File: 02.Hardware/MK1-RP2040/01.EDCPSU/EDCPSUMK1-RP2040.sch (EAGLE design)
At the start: 182 parts, among them J6 Display, Q2 2N7002PW, Q4 2N7002PW, Q9 2N7002PW, U1 RP2040TR7, U11 AP63203, U12 AP64501SP-13, U2 MCP4725, U3 SN74AC14PWR, U4 MAX9938FEUK+T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

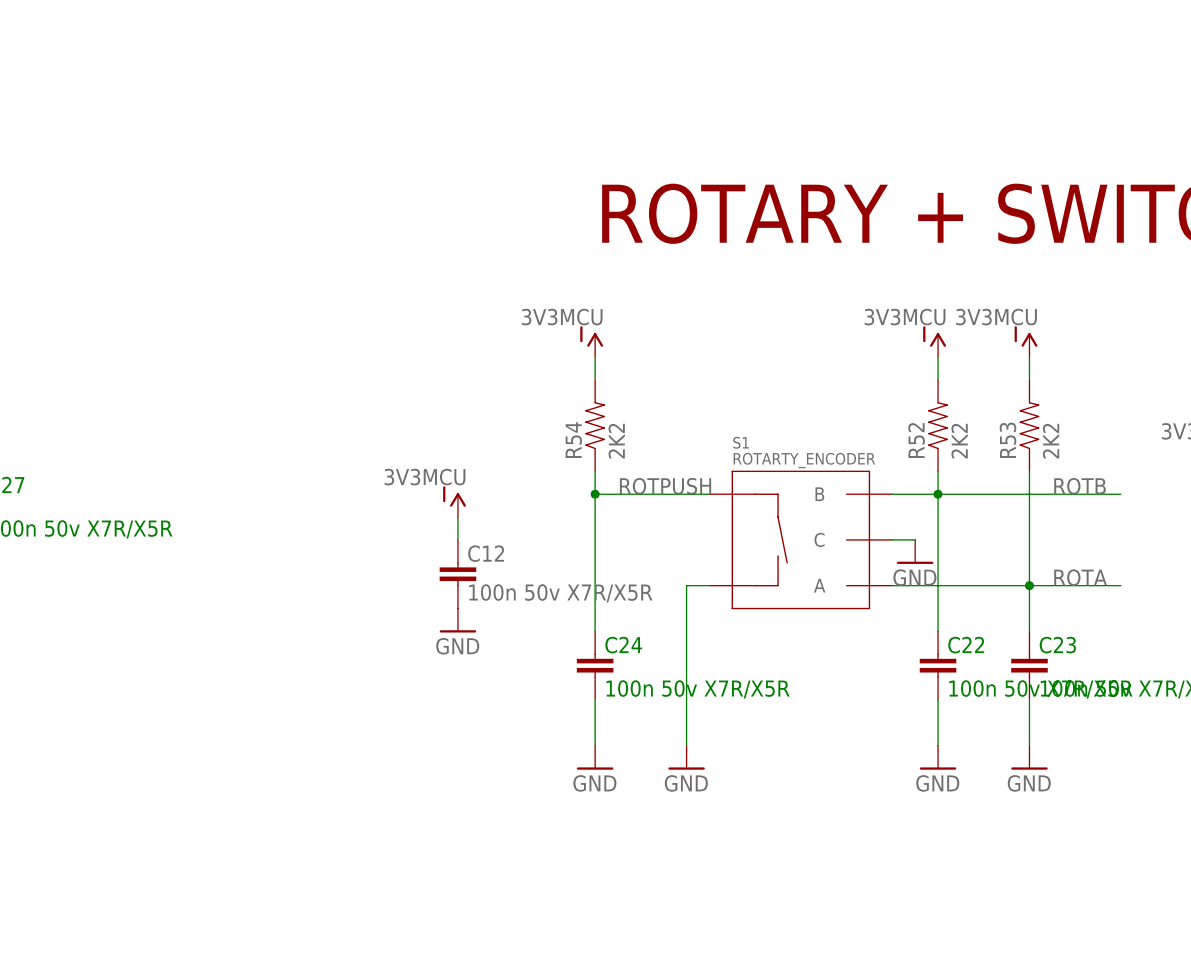
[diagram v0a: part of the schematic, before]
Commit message: Actualizacion BOM MK1 RP2040 y cambios menores
Se agranda los agujeros laterales del rotary.
Intercambio de posición de las vías del pedal.
Acortamiento de la peninsula.
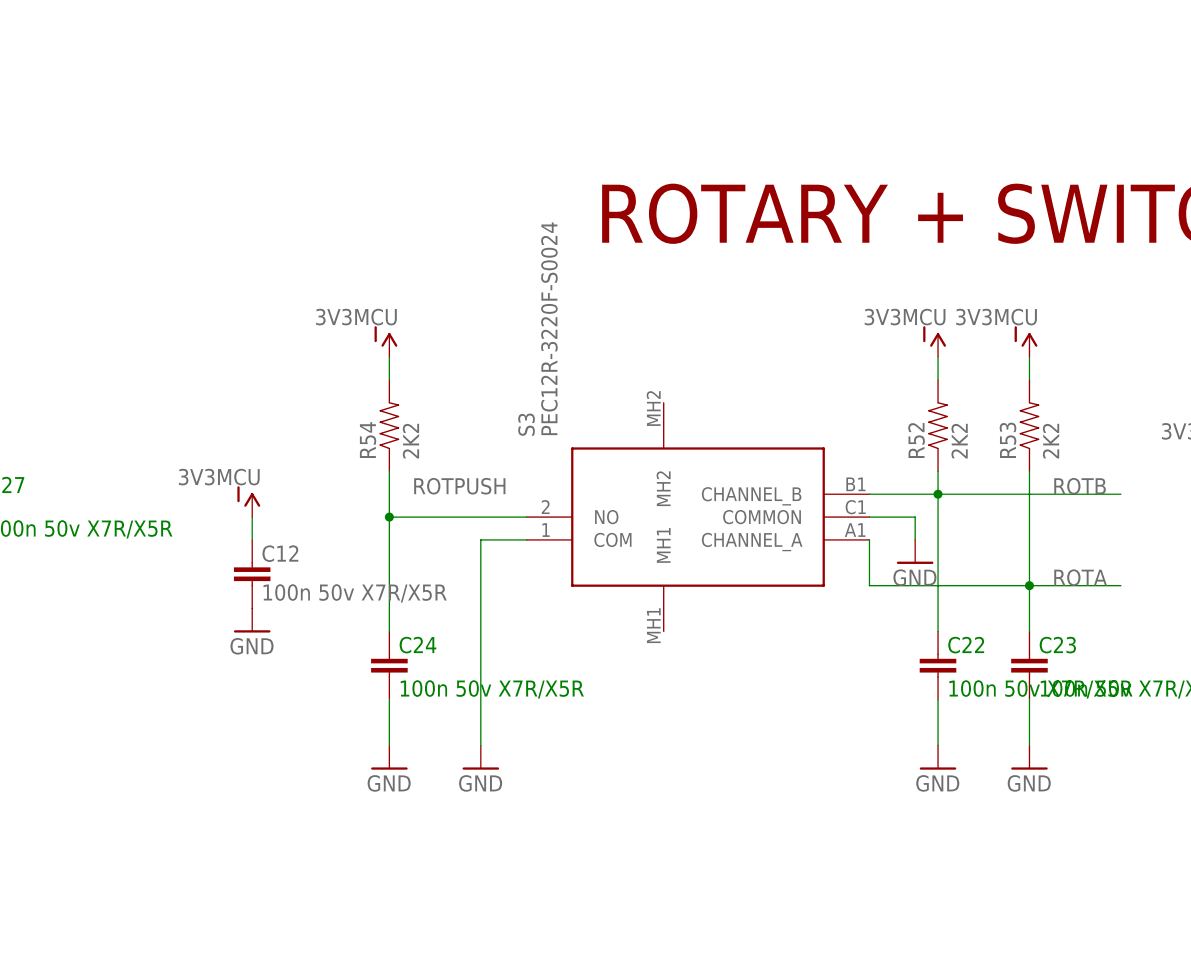
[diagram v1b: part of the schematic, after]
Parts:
- removed S1: ROTARTY_ENCODER, SparkFun-Electromechanical:ROTARTY_ENCODER
- added S3: PEC12R-3220F-S0024, PEC12R-3220F-S0024:PEC12R-3220F-S0024
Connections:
- net GND: now also S3.COM, S3.COMMON; no longer S1.C, S1.SW-
- net ROTA: now also S3.CHANNEL_A; no longer S1.A
- net ROTB: now also S3.CHANNEL_B; no longer S1.B
- net ROTPUSH: now also S3.NO; no longer S1.SW+
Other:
- moved on the sheet: C12, C24, R54
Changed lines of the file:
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@@
 </classes>
 <parts>
-<part name="S1" library="SparkFun-Electromechanical" deviceset="ROTARTY_ENCODER" device=""/>
 <part name="R28" library="SparkFun-Resistors" library_urn="urn:adsk.eagle:library:532" deviceset="RESISTOR" device="0805" package3d_urn="urn:adsk.eagle:package:39651/1" value="33R"/>
 <part name="GND30" library="SparkFun" deviceset="GND" device=""/>
@@
 <part name="U$42" library="SparkFun-Aesthetics" deviceset="VCC-ISO" device="" value="3V3MCU"/>
 <part name="U$43" library="SparkFun-Aesthetics" deviceset="VCC-ISO" device="" value="3V3MCU"/>
+<part name="S3" library="PEC12R-3220F-S0024" deviceset="PEC12R-3220F-S0024" device=""/>
 </parts>
 <sheets>
@@
 </plain>
 <instances>
-<instance part="S1" gate="G$1" x="-60.96" y="350.52" smashed="yes">
-<attribute name="NAME" x="-68.58" y="360.68" size="1.27" layer="95"/>
-<attribute name="VALUE" x="-68.58" y="358.902" size="1.27" layer="96"/>
-</instance>
 <instance part="R28" gate="G$1" x="-172.72" y="327.66" smashed="yes" rot="R180">
 <attribute name="NAME" x="-168.91" y="326.1614" size="1.778" layer="95" rot="R180"/>
@@
 <attribute name="VALUE" x="-38.1" y="322.58" size="1.778" layer="96"/>
 </instance>
-<instance part="R54" gate="G$1" x="-83.82" y="363.22" smashed="yes" rot="R90">
-<attribute name="NAME" x="-85.3186" y="359.41" size="1.778" layer="95" rot="R90"/>
-<attribute name="VALUE" x="-80.518" y="359.41" size="1.778" layer="96" rot="R90"/>
-</instance>
-<instance part="C24" gate="G$1" x="-83.82" y="337.82" smashed="yes" rot="R180">
-<attribute name="NAME" x="-82.804" y="337.947" size="1.778" layer="91"/>
-<attribute name="VALUE" x="-82.804" y="333.121" size="1.778" layer="91"/>
-</instance>
-<instance part="GND42" gate="1" x="-83.82" y="325.12" smashed="yes">
-<attribute name="VALUE" x="-86.36" y="322.58" size="1.778" layer="96"/>
-</instance>
-<instance part="GND43" gate="1" x="-73.66" y="325.12" smashed="yes">
-<attribute name="VALUE" x="-76.2" y="322.58" size="1.778" layer="96"/>
+<instance part="R54" gate="G$1" x="-106.68" y="363.22" smashed="yes" rot="R90">
+<attribute name="NAME" x="-108.1786" y="359.41" size="1.778" layer="95" rot="R90"/>
+<attribute name="VALUE" x="-103.378" y="359.41" size="1.778" layer="96" rot="R90"/>
+</instance>
+<instance part="C24" gate="G$1" x="-106.68" y="337.82" smashed="yes" rot="R180">
+<attribute name="NAME" x="-105.664" y="337.947" size="1.778" layer="91"/>
+<attribute name="VALUE" x="-105.664" y="333.121" size="1.778" layer="91"/>
+</instance>
+<instance part="GND42" gate="1" x="-106.68" y="325.12" smashed="yes">
+<attribute name="VALUE" x="-109.22" y="322.58" size="1.778" layer="96"/>
+</instance>
+<instance part="GND43" gate="1" x="-96.52" y="325.12" smashed="yes">
+<attribute name="VALUE" x="-99.06" y="322.58" size="1.778" layer="96"/>
 </instance>
 <instance part="GND48" gate="1" x="2.54" y="322.58" smashed="yes">
@@
 <attribute name="VALUE" x="7.62" y="320.04" size="1.778" layer="96"/>
 </instance>
-<instance part="U$2" gate="G$1" x="-83.82" y="370.84" smashed="yes" rot="MR0">
-<attribute name="VALUE" x="-82.804" y="374.396" size="1.778" layer="96" rot="MR0"/>
+<instance part="U$2" gate="G$1" x="-106.68" y="370.84" smashed="yes" rot="MR0">
+<attribute name="VALUE" x="-105.664" y="374.396" size="1.778" layer="96" rot="MR0"/>
 </instance>
 <instance part="U$19" gate="G$1" x="-45.72" y="370.84" smashed="yes" rot="MR0">
@@
 <attribute name="VALUE" x="-11.684" y="348.869" size="1.778" layer="96"/>
 </instance>
-<instance part="C12" gate="G$1" x="-99.06" y="347.98" smashed="yes" rot="R180">
-<attribute name="NAME" x="-98.044" y="348.107" size="1.778" layer="95"/>
-<attribute name="VALUE" x="-98.044" y="343.789" size="1.778" layer="96"/>
+<instance part="C12" gate="G$1" x="-121.92" y="347.98" smashed="yes" rot="R180">
+<attribute name="NAME" x="-120.904" y="348.107" size="1.778" layer="95"/>
+<attribute name="VALUE" x="-120.904" y="343.789" size="1.778" layer="96"/>
 </instance>
 <instance part="U$3" gate="G$1" x="-12.7" y="358.14" smashed="yes" rot="MR0">
 <attribute name="VALUE" x="-11.684" y="361.696" size="1.778" layer="96" rot="MR0"/>
 </instance>
-<instance part="U$14" gate="G$1" x="-99.06" y="353.06" smashed="yes" rot="MR0">
-<attribute name="VALUE" x="-98.044" y="356.616" size="1.778" layer="96" rot="MR0"/>
-</instance>
-<instance part="GND2" gate="1" x="-99.06" y="340.36" smashed="yes">
-<attribute name="VALUE" x="-101.6" y="337.82" size="1.778" layer="96"/>
+<instance part="U$14" gate="G$1" x="-121.92" y="353.06" smashed="yes" rot="MR0">
+<attribute name="VALUE" x="-120.904" y="356.616" size="1.778" layer="96" rot="MR0"/>
+</instance>
+<instance part="GND2" gate="1" x="-121.92" y="340.36" smashed="yes">
+<attribute name="VALUE" x="-124.46" y="337.82" size="1.778" layer="96"/>
 </instance>
 <instance part="GND20" gate="1" x="-12.7" y="345.44" smashed="yes">
@@
 <instance part="U$43" gate="G$1" x="-241.3" y="236.22" smashed="yes">
 <attribute name="VALUE" x="-242.316" y="239.776" size="1.778" layer="96"/>
+</instance>
+<instance part="S3" gate="G$1" x="-76.2" y="340.36" smashed="yes" rot="R90">
+<attribute name="NAME" x="-91.44" y="361.95" size="1.778" layer="95" rot="R90" align="center-left"/>
+<attribute name="VALUE" x="-88.9" y="361.95" size="1.778" layer="96" rot="R90" align="center-left"/>
 </instance>
 </instances>
@@
 </segment>
 <segment>
-<pinref part="S1" gate="G$1" pin="C"/>
-<pinref part="GND38" gate="1" pin="GND"/>
-<wire x1="-50.8" y1="350.52" x2="-48.26" y2="350.52" width="0.1524" layer="91"/>
-</segment>
-<segment>
 <pinref part="C24" gate="G$1" pin="1"/>
 <pinref part="GND42" gate="1" pin="GND"/>
-<wire x1="-83.82" y1="327.66" x2="-83.82" y2="332.74" width="0.1524" layer="91"/>
+<wire x1="-106.68" y1="327.66" x2="-106.68" y2="332.74" width="0.1524" layer="91"/>
 </segment>
 <segment>
@@
 <segment>
 <pinref part="GND43" gate="1" pin="GND"/>
-<wire x1="-73.66" y1="327.66" x2="-73.66" y2="345.44" width="0.1524" layer="91"/>
-<pinref part="S1" gate="G$1" pin="SW-"/>
-<wire x1="-73.66" y1="345.44" x2="-71.12" y2="345.44" width="0.1524" layer="91"/>
+<wire x1="-96.52" y1="327.66" x2="-96.52" y2="350.52" width="0.1524" layer="91"/>
+<pinref part="S3" gate="G$1" pin="COM"/>
+<wire x1="-91.44" y1="350.52" x2="-96.52" y2="350.52" width="0.1524" layer="91"/>
 </segment>
 <segment>
@@
 <label x="-375.92" y="337.82" size="1.778" layer="95"/>
 </segment>
+<segment>
+<pinref part="GND38" gate="1" pin="GND"/>
+<pinref part="S3" gate="G$1" pin="COMMON"/>
+<wire x1="-48.26" y1="350.52" x2="-48.26" y2="353.06" width="0.1524" layer="91"/>
+<wire x1="-48.26" y1="353.06" x2="-53.34" y2="353.06" width="0.1524" layer="91"/>
+</segment>
 </net>
 <net name="N$20" class="0">
@@
 <segment>
 <pinref part="R54" gate="G$1" pin="1"/>
-<wire x1="-83.82" y1="358.14" x2="-83.82" y2="355.6" width="0.1524" layer="91"/>
 <pinref part="C24" gate="G$1" pin="2"/>
-<pinref part="S1" gate="G$1" pin="SW+"/>
-<wire x1="-83.82" y1="355.6" x2="-83.82" y2="340.36" width="0.1524" layer="91"/>
-<wire x1="-71.12" y1="355.6" x2="-83.82" y2="355.6" width="0.1524" layer="91"/>
-<junction x="-83.82" y="355.6"/>
-<label x="-81.28" y="355.6" size="1.778" layer="95"/>
+<wire x1="-106.68" y1="358.14" x2="-106.68" y2="353.06" width="0.1524" layer="91"/>
+<label x="-104.14" y="355.6" size="1.778" layer="95"/>
+<pinref part="S3" gate="G$1" pin="NO"/>
+<wire x1="-106.68" y1="353.06" x2="-106.68" y2="340.36" width="0.1524" layer="91"/>
+<wire x1="-91.44" y1="353.06" x2="-106.68" y2="353.06" width="0.1524" layer="91"/>
+<junction x="-106.68" y="353.06"/>
 </segment>
 <segment>
@@
 <pinref part="C23" gate="G$1" pin="2"/>
 <wire x1="-35.56" y1="358.14" x2="-35.56" y2="345.44" width="0.1524" layer="91"/>
-<pinref part="S1" gate="G$1" pin="A"/>
 <wire x1="-35.56" y1="345.44" x2="-35.56" y2="340.36" width="0.1524" layer="91"/>
-<wire x1="-50.8" y1="345.44" x2="-35.56" y2="345.44" width="0.1524" layer="91"/>
 <junction x="-35.56" y="345.44"/>
 <wire x1="-35.56" y1="345.44" x2="-25.4" y2="345.44" width="0.1524" layer="91"/>
 <label x="-33.02" y="345.44" size="1.778" layer="95"/>
+<pinref part="S3" gate="G$1" pin="CHANNEL_A"/>
+<wire x1="-53.34" y1="350.52" x2="-53.34" y2="345.44" width="0.1524" layer="91"/>
+<wire x1="-53.34" y1="345.44" x2="-35.56" y2="345.44" width="0.1524" layer="91"/>
 </segment>
 <segment>
@@
 <net name="ROTB" class="0">
 <segment>
-<pinref part="S1" gate="G$1" pin="B"/>
 <pinref part="R52" gate="G$1" pin="1"/>
-<wire x1="-50.8" y1="355.6" x2="-45.72" y2="355.6" width="0.1524" layer="91"/>
 <wire x1="-45.72" y1="355.6" x2="-45.72" y2="358.14" width="0.1524" layer="91"/>
 <pinref part="C22" gate="G$1" pin="2"/>
@@
 <wire x1="-45.72" y1="355.6" x2="-25.4" y2="355.6" width="0.1524" layer="91"/>
 <label x="-33.02" y="355.6" size="1.778" layer="95"/>
+<pinref part="S3" gate="G$1" pin="CHANNEL_B"/>
+<wire x1="-53.34" y1="355.6" x2="-45.72" y2="355.6" width="0.1524" layer="91"/>
 </segment>
 <segment>
@@
 <segment>
 <pinref part="R54" gate="G$1" pin="2"/>
-<wire x1="-83.82" y1="370.84" x2="-83.82" y2="368.3" width="0.1524" layer="91"/>
+<wire x1="-106.68" y1="370.84" x2="-106.68" y2="368.3" width="0.1524" layer="91"/>
 <pinref part="U$2" gate="G$1" pin="VCC-ISO"/>
 </segment>
@@
 <pinref part="C12" gate="G$1" pin="2"/>
 <pinref part="U$14" gate="G$1" pin="VCC-ISO"/>
-<wire x1="-99.06" y1="353.06" x2="-99.06" y2="350.52" width="0.1524" layer="91"/>
-</segment>
-<segment>
+<wire x1="-121.92" y1="353.06" x2="-121.92" y2="350.52" width="0.1524" layer="91"/>
+</segment>
+<segment>

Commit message: Cierra issue #2 y revision general para peticion de fabricacion SETI
Revision general.
Se añade detalles menores.
Cierra issue #2
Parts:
- added C1: 100n 50v X7R/X5R, SparkFun-Passives:CAP0805
- added IN_OVC: TESTPAD_TPSQB1,27, BeagleBone_Blue_R3:TESTPAD_TPSQB1,27
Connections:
- net 3V3MCU: now also C1.2
- net GND: now also C1.1
- net IN_OVC: now also IN_OVC.TP
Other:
- note added: "INPUT POWER"
- note added: "MK1-RP2040 v1-Jan-2023"
- note added: "Opcional para usar con LDO que sea Ajustable"
- note removed: "MK2-RP2040 v2-May-2023"
- moved on the sheet: BZ1, C10, C12, C13, C14, C15, C16, C17, C18, C19, C2, C20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

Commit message: PCB MK1 RP2040- Pines RX TX
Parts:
- added RX, TX: TESTPAD_TPSQB1,27, BeagleBone_Blue_R3:TESTPAD_TPSQB1,27
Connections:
- net RX: now also RX.TP
- net TX: now also TX.TP
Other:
- note added: "MK1-RP2040 v2-Abr-2024"
- note removed: "MK1-RP2040 v1-Jan-2023"
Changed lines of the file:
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@@
 <part name="C1" library="SparkFun-Passives" deviceset="CAP" device="0805" value="100n 50v X7R/X5R"/>
 <part name="IN_OVC" library="BeagleBone_Blue_R3" deviceset="TESTPAD_TPSQ" device="B1,27"/>
+<part name="RX" library="BeagleBone_Blue_R3" deviceset="TESTPAD_TPSQ" device="B1,27"/>
+<part name="TX" library="BeagleBone_Blue_R3" deviceset="TESTPAD_TPSQ" device="B1,27"/>
 </parts>
 <sheets>
@@
 <text x="-622.3" y="43.18" size="6.4516" layer="94">TEST PADS</text>
 <text x="-320.04" y="429.26" size="11.5316" layer="94">MK1-RP2040
-v1-Jan-2023</text>
+v2-Abr-2024</text>
 <text x="50.8" y="335.28" size="1.778" layer="94">(DATA/COMMAND)</text>
 <text x="-66.04" y="383.54" size="1.778" layer="91">Overlap buzzer assy concentric</text>
@@
 <attribute name="TP_SIGNAL_NAME" x="-560.62" y="-12.7012" size="1.778" layer="97" rot="R270"/>
 </instance>
+<instance part="RX" gate="G$1" x="-620.31" y="-15.2412" smashed="yes" rot="R270">
+<attribute name="TP_SIGNAL_NAME" x="-621.58" y="-17.7812" size="1.778" layer="97" rot="R270"/>
+</instance>
+<instance part="TX" gate="G$1" x="-620.31" y="-10.1612" smashed="yes" rot="R270">
+<attribute name="TP_SIGNAL_NAME" x="-621.58" y="-12.7012" size="1.778" layer="97" rot="R270"/>
+</instance>
 </instances>
 <busses>
@@
 <label x="-266.7" y="200.66" size="1.778" layer="95"/>
 </segment>
+<segment>
+<wire x1="-617.22" y1="-10.16" x2="-599.44" y2="-10.16" width="0.1524" layer="91"/>
+<pinref part="TX" gate="G$1" pin="TP"/>
+<wire x1="-617.77" y1="-10.1612" x2="-617.22" y2="-10.1612" width="0.1524" layer="91"/>
+<wire x1="-617.22" y1="-10.1612" x2="-617.22" y2="-10.16" width="0.1524" layer="91"/>
+<label x="-612.14" y="-10.16" size="1.778" layer="95"/>
+</segment>
 </net>
 <net name="RX" class="0">
@@
 <label x="-266.7" y="198.12" size="1.778" layer="95"/>
 </segment>
+<segment>
+<pinref part="RX" gate="G$1" pin="TP"/>
+<wire x1="-617.77" y1="-15.2412" x2="-617.77" y2="-15.24" width="0.1524" layer="91"/>
+<wire x1="-617.77" y1="-15.24" x2="-599.44" y2="-15.24" width="0.1524" layer="91"/>
+<label x="-612.14" y="-15.24" size="1.778" layer="95"/>
+</segment>
 </net>
 <net name="N$82" class="0">
@@
 <net name="N$50" class="0">
 <segment>
-<wire x1="228.6" y1="152.4" x2="228.6" y2="50.8" width="0.1524" layer="91" style="shortdash"/>
-<wire x1="228.6" y1="50.8" x2="520.7" y2="50.8" width="0.1524" layer="91" style="shortdash"/>
+<wire x1="228.6" y1="149.86" x2="228.6" y2="48.26" width="0.1524" layer="91" style="shortdash"/>
+<wire x1="228.6" y1="48.26" x2="520.7" y2="50.8" width="0.1524" layer="91" style="shortdash"/>
 <wire x1="520.7" y1="50.8" x2="520.7" y2="152.4" width="0.1524" layer="91" style="shortdash"/>
-<wire x1="520.7" y1="152.4" x2="228.6" y2="152.4" width="0.1524" layer="91" style="shortdash"/>
+<wire x1="520.7" y1="152.4" x2="228.6" y2="149.86" width="0.1524" layer="91" style="shortdash"/>
 </segment>
 </net>
